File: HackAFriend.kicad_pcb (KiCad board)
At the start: 2 copper layers, 135 x 59 mm, 102 parts, among them J1 PRT-14417, J10 Conn_01x16, J11 USB_C_Receptacle_USB2.0_16P, J3 Conn_01x02, J4 Conn_01x02, J5 Conn_01x02, J7 Conn_01x02, J8 Conn_01x12, J9 Conn_01x02, P1 TC2050-IDC, SW1 GP0115ACCG30, SW10 SPST_BTN_A, SW11 SPST_BTN_X, SW12 SPST_BTN_Y, SW2 SW_SPST, SW3 SPST_DPAD_LEFT, SW4 SPST_BTN_SELECT, SW5 SPST_DPAD_DOWN, SW6 SPST_DPAD_RIGHT, SW7 SPST_DPAD_UP, SW8 SPST_DPAD_START, SW9 SPST_BTN_B, U1 DA7282-00FVC, U3 W25Q64JVSSIQ, U4 MCP23017_ML, U6 BQ24072RGT, U7 MAX98357A, U8 NJM2884U1-33-TE1, U9 MDBT50Q-1MV2, Y1 ABS06-32.768KHZ-1-T

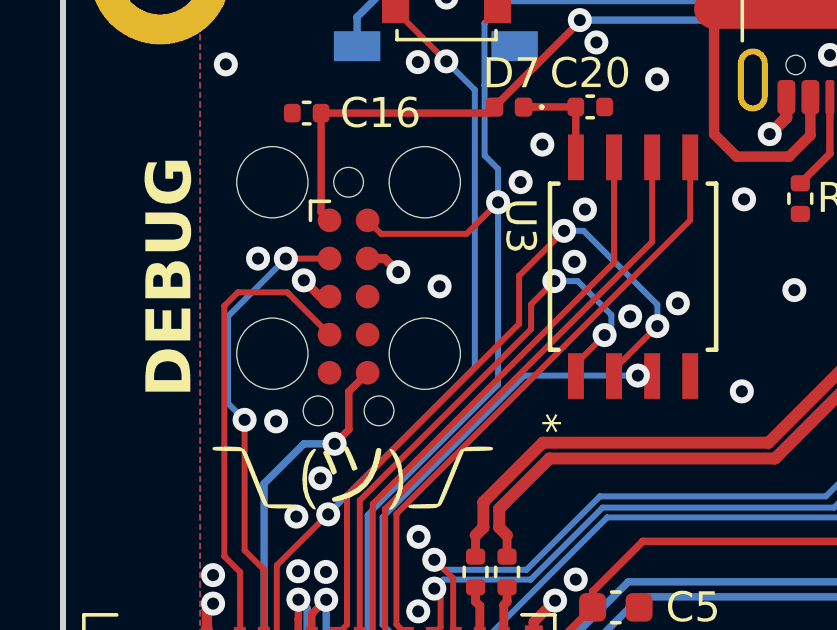
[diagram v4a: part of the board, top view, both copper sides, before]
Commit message: Tweak locations and add a bypass capacitor for VBUS
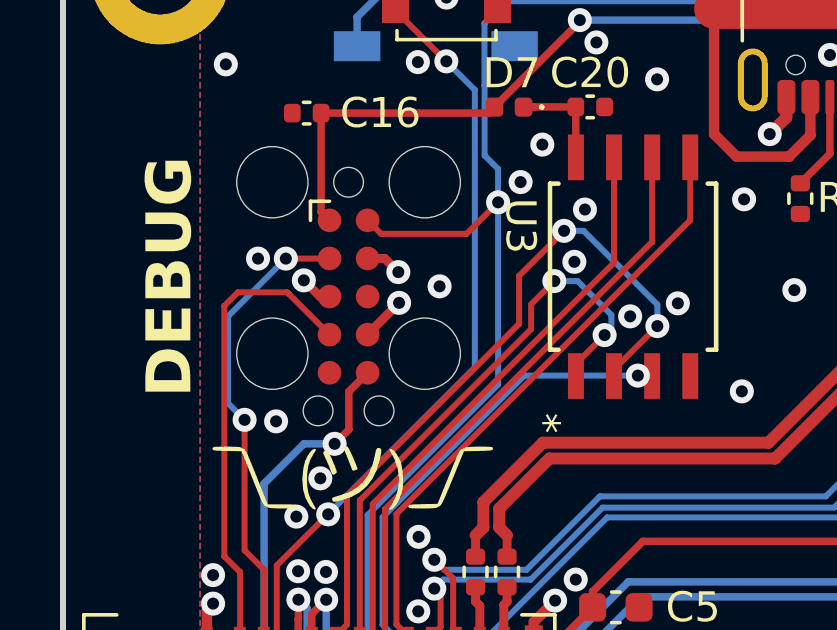
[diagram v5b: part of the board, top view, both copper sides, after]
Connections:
- P1 pad 7: unconnected-(P1-P7-Pad7) -> GND
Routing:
- net GND: track 38.5 -> 40.0 mm, vias 259 -> 260

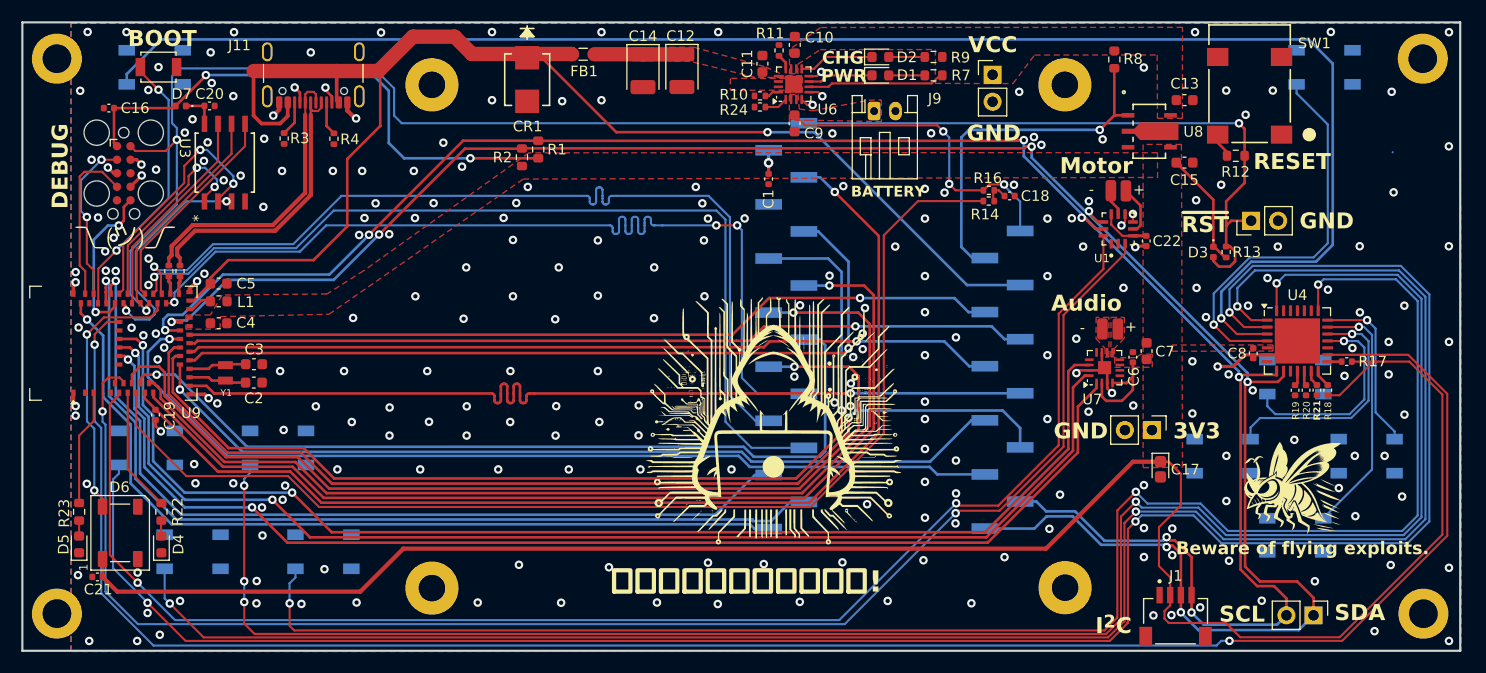
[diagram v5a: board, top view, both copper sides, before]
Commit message: Replaced DA7280 with DRV2605
Replaced DA7280 with DRV2605 to simplify board support code in Hack-A-Friend Arduino Library.
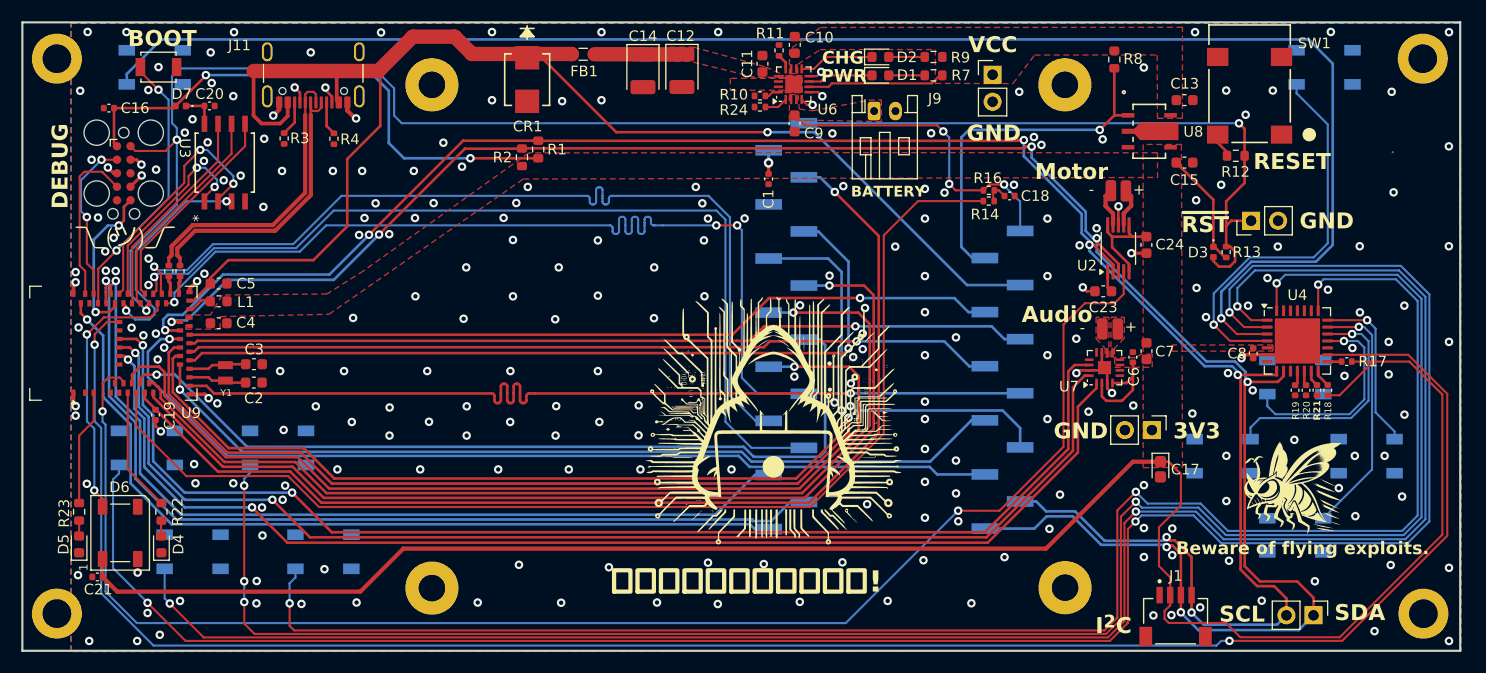
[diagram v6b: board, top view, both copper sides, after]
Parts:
- removed C22: 0.1uF, Capacitor_SMD:C_0402_1005Metric
- removed U1: DA7282-00FVC, DA7282_00FVC:QFN65P300X300X84-12N
- added C23: 1uF, Capacitor_SMD:C_0603_1608Metric, F.Cu at (182.5, 86.7)
- added C24: 1uF, Capacitor_SMD:C_0603_1608Metric, F.Cu at (186.6, 82.4)
- added U2: DRV2605LDGS, Package_SO:VSSOP-10_3x3mm_P0.5mm, F.Cu at (184.0, 82.7)
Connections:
- U9 pad 6: /Human Interfaces/MOTOR_DRV.IRQ -> unconnected-(U9-P1.13-Pad6)
- U9 pad 7: /Human Interfaces/MOTOR_DRV.GPI0 -> /Human Interfaces/MOTOR_PWM
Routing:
- net /Human Interfaces/MOTOR_DRV.GPI0: track 141.7 -> 0.00 mm, vias 2 -> 0
- net /Human Interfaces/MOTOR_PWM: track 0.00 -> 140.6 mm, vias 0 -> 2
- net /Human Interfaces/MOTOR_DRV.IRQ: track 135.6 -> 0.00 mm, vias 2 -> 0
- net +3V3: track 262.0 -> 267.2 mm
- net /Connectors/I2C_BUS.SDA: track 191.4 -> 195.1 mm
- net /Connectors/I2C_BUS.SCL: track 187.3 -> 189.4 mm
- net Net-(U2-REG): track 0.00 -> 1.97 mm
- net /Human Interfaces/MOTOR_OUT-: track 2.49 -> 3.72 mm
- net GND: track 40.0 -> 38.8 mm, vias 260 -> 257
- net /Human Interfaces/MOTOR_OUT+: track 4.66 -> 3.70 mm
